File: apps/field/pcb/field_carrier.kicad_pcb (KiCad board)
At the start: 2 copper layers, 55 x 72 mm, 5 parts, among them J1 XIAO_ESP32C6, J3 E220_EV2, J4 ログ_UART0

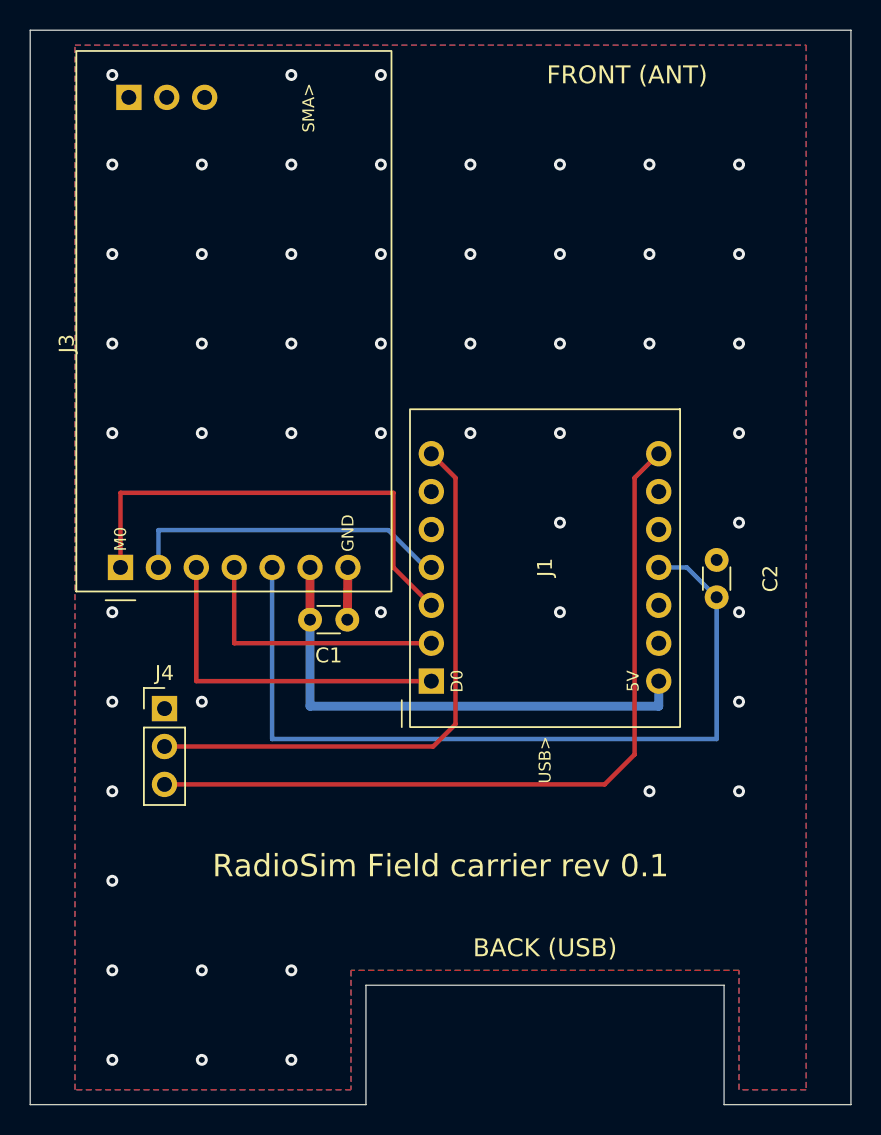
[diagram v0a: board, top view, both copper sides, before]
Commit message: feat(field): 台を EXPE7-4-6 に合わせて 55×45 で作り直し、表示の LED（D1〜D3・R1〜R6）を回路図と基板に足す
- 回路図: XIAO の D4・D5（920 の送信・受信）と D8・D9（2.4 の送信・受信）を 330 Ω 経由で
  D2・D3（OSRGHC3132A・赤＝送信・緑＝受信）へ。D1＝電源（5V から 1 kΩ×2・赤と黄緑で黄）。ERC 0 件
- 基板: 外形 55.0×45.0（切り欠きなし）。XIAO は基板の縁を y 45.5（受け口の面が背面パネルの外面と面一）。
  LED は背面の端（x 9.0・14.08・19.16・ランドの列 y 43.73）。抵抗は EV2 の下（EV2 は約 11 mm 浮く）に
  2.54 間隔＝LED の足から 7 ピンの隙間を真っすぐ通る。C1 は EV2 の 6・7 番の前、C2 は XIAO の右、J4 は右前
- 専用フットプリント: LED_D3.0mm-3_Horizontal_Staggered を足した（ランド 1.5＝背面端まで 0.5 を守る）。
  XIAO は受け口が縁から 2 mm 出る分を込み合いの枠に足し、シルクを台の上に収めた。EV2 の込み合いの枠は
  ソケットだけ（下に低い部品を置けるように）
- DRC（回路図との照合つき）＝違反 0・未配線 0・不一致 0

HARDWARE.md §3・§4 と wiring.svg はまだ直していない（次の作業）。

Co-Authored-By: Claude Opus 5.5 <noreply@anthropic.com>
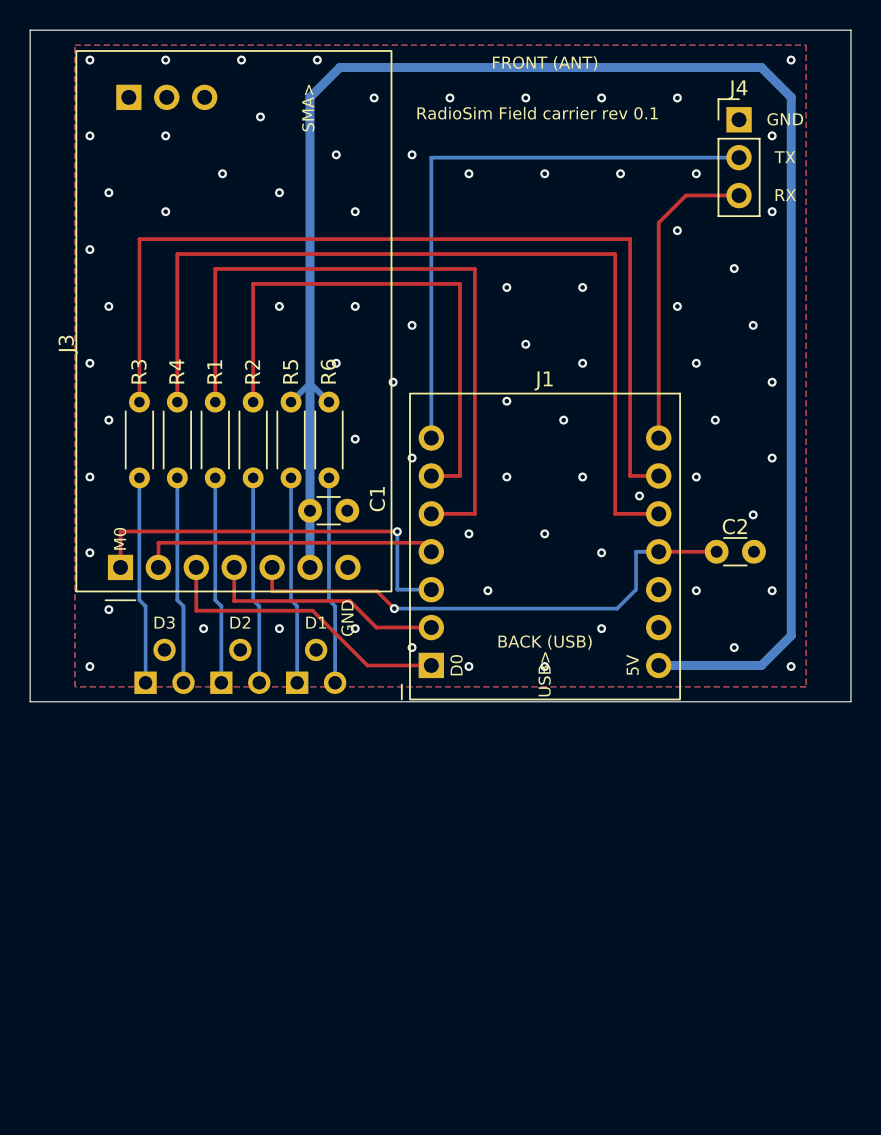
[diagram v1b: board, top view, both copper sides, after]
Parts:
- added D1: OSRGHC3132A, field_carrier:LED_D3.0mm-3_Horizontal_Staggered, F.Cu at (69.2, 73.7)
- added D2: OSRGHC3132A, field_carrier:LED_D3.0mm-3_Horizontal_Staggered, F.Cu at (64.1, 73.7)
- added D3: OSRGHC3132A, field_carrier:LED_D3.0mm-3_Horizontal_Staggered, F.Cu at (59.0, 73.7)
- added R1: 330, Resistor_THT:R_Axial_DIN0204_L3.6mm_D1.6mm_P5.08mm_Horizontal, F.Cu at (62.4, 54.9)
- added R2: 330, Resistor_THT:R_Axial_DIN0204_L3.6mm_D1.6mm_P5.08mm_Horizontal, F.Cu at (64.9, 54.9)
- added R3: 330, Resistor_THT:R_Axial_DIN0204_L3.6mm_D1.6mm_P5.08mm_Horizontal, F.Cu at (57.3, 54.9)
- added R4: 330, Resistor_THT:R_Axial_DIN0204_L3.6mm_D1.6mm_P5.08mm_Horizontal, F.Cu at (59.9, 54.9)
- added R5: 1k, Resistor_THT:R_Axial_DIN0204_L3.6mm_D1.6mm_P5.08mm_Horizontal, F.Cu at (67.5, 54.9)
- added R6: 1k, Resistor_THT:R_Axial_DIN0204_L3.6mm_D1.6mm_P5.08mm_Horizontal, F.Cu at (70.0, 54.9)
- moved J4 55.1 mm to (97.5, 36.0)
- moved C1 7.30 mm to (68.8, 62.2)
- moved C2 3.05 mm to (96.0, 65.0), turned to 0 degrees
- moved J1 1.05 mm to (84.5, 65.0)
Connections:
- J1 pad 10: unconnected-(J1B-D9-Pad10) -> /LED24_RX
- J1 pad 5: unconnected-(J1A-D4-Pad5) -> /LED920_TX
- J1 pad 6: unconnected-(J1A-D5-Pad6) -> /LED920_RX
- J1 pad 9: unconnected-(J1B-D8-Pad9) -> /LED24_TX
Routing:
- net +5V: track 34.3 -> 114.8 mm
- net /LED24_TX: track 0.00 -> 61.6 mm
- net /LED24_RX: track 0.00 -> 59.6 mm
- net /LED920_TX: track 0.00 -> 45.6 mm
- net /LED920_RX: track 0.00 -> 36.6 mm
- net /LOG_RX: track 53.2 -> 20.6 mm
- net /EV2_AUX: track 55.5 -> 34.9 mm, vias 0 -> 1
- net Net-(D1-A2): track 0.00 -> 13.9 mm
- net Net-(D3-A2): track 0.00 -> 13.9 mm
- net Net-(D2-A1): track 0.00 -> 13.9 mm
- net Net-(D3-A1): track 0.00 -> 13.9 mm
- net Net-(D1-A1): track 0.00 -> 13.9 mm
- net Net-(D2-A2): track 0.00 -> 13.9 mm
- net /EV2_M0: track 31.9 -> 27.1 mm, vias 0 -> 1
- net GND: track 3.50 -> 0.00 mm, vias 53 -> 75
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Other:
- board size 55 x 72 mm -> 55 x 45 mm
- board text added: "GND"
- board text added: "RX"
- board text added: "TX"

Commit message: feat(field): 表示の LED を 1 列のフットプリントへ置き換え、アノードと EV2_RXD を引き直す
- 専用フットプリントを LED_D3.0mm-3_Horizontal_Staggered（三角）から
  LED_D3.0mm-3_Horizontal_O2.54mm_Z2.0mm（足 3 本を 2.54 間隔の 1 列）へ。
  曲げる位置はつばから 2.54＝データシートの樹脂のはみ出し（1.5MAX）と外側の足の開き
  （つばの下 約 1.1 で 2.54 に開き終わる）の両方から外れる。軸の高さ Z 2.0 とつばを
  背面パネルの内面に当てる位置は前のまま
- 配置: D3・D2・D1＝中心 x 8.45・15.25・22.05、ランドの列 y 42.46（6.8 間隔・ランド 1.5）。
  D3 の穴の縁 6.85 は穴あけ範囲（有効寸法 41.5）の左端 6.75 まで 0.1。外側のフレームの
  窓の縁（図面 p002 の正面図を画素で測った・LED の軸の高さで x 5.59）までは 約 1.26
- 裏: アノード 6 本は y 41.4 から 45° でそろえて寄せ、EV2 の 7 ピンの隙間を抜けて抵抗へ
  （抵抗の並びは前のまま）。表: EV2_RXD は XIAO の 1 番から斜めに下げ、LED のランドの前
  （y 40.93）を通って TXD の外を回る
- 新しい線に乗った GND の縫いビア 3 つを除いた（75 → 72）。XIAO の込み合いの枠は
  EV2 と同じくソケットの 2 列だけにした（モジュールは約 11 mm 浮く・LED は高さ 約 3.9）
- DRC（回路図との照合つき）＝違反 0・未配線 0・不一致 0。ERC 0

Co-Authored-By: Claude Opus 5.5 <noreply@anthropic.com>
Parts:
- D1, D2, D3: footprint field_carrier:LED_D3.0mm-3_Horizontal_Staggered -> field_carrier:LED_D3.0mm-3_Horizontal_O2.54mm_Z2.0mm
- moved D1 3.16 mm to (72.0, 72.5)
- moved D2 1.73 mm to (65.2, 72.5)
- moved D3 1.38 mm to (58.5, 72.5)
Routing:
- net Net-(D2-A1): track 13.9 -> 12.6 mm
- net Net-(D3-A2): track 13.9 -> 12.9 mm
- net Net-(D3-A1): track 13.9 -> 13.0 mm
- net Net-(D1-A1): track 13.9 -> 13.3 mm
- net GND: vias 75 -> 72

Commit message: feat(field): 台を背面パネルまで伸ばし（55.0×46.0）、溝に入る両端の帯を GND として露出してケースを接地する
- 台の後端 45.0 → 46.0（前後のパネルの内面どうし）＝ケーブルを挿す力を XIAO でなくパネルで受ける
- 溝に入る帯（両端から 0.5〜2.5 mm）を表裏とも GND のベタにしてレジストを抜き、縫いビアを片側 9 個足した
- J3 の番号を EV2 の外形の内側へ移した（溝の帯に掛かっていた）
- HARDWARE.md の §4 に台とケースの行と「台とケース」の小節、wiring.svg に「台とケース」の節を足した

Co-Authored-By: Claude Opus 5.5 <noreply@anthropic.com>
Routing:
- net GND: vias 72 -> 90
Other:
- board size 55 x 45 mm -> 55 x 46 mm
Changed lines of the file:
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@@
 		(descr "CLEALINK E220-900T22S(JP)-EV2 (board 10060-V1.1), 36.00x20.90 mm. Pins 1-7 = M0 M1 RXD TXD AUX VCC GND; pins 8-10 = GND through-holes, 31.50 mm from the pin row. No mounting holes. Courtyard covers the sockets only: the module sits about 11 mm above the carrier, so low parts (resistors, C1) may go under it.")
 		(property "Reference" "J3"
-			(at 15 -3.6 90)
+			(at 26 -1.75 90)
 			(layer "F.SilkS")
 			(effects
@@
 		)
 	)
+	(gr_rect
+		(start 50.5 30.5)
+		(end 52.5 75.5)
+		(stroke
+			(width 0)
+			(type solid)
+		)
+		(fill yes)
+		(layer "F.Mask")
+	)
+	(gr_rect
+		(start 102.5 30.5)
+		(end 104.5 75.5)
+		(stroke
+			(width 0)
+			(type solid)
+		)
+		(fill yes)
+		(layer "F.Mask")
+	)
+	(gr_rect
+		(start 50.5 30.5)
+		(end 52.5 75.5)
+		(stroke
+			(width 0)
+			(type solid)
+		)
+		(fill yes)
+		(layer "B.Mask")
+	)
+	(gr_rect
+		(start 102.5 30.5)
+		(end 104.5 75.5)
+		(stroke
+			(width 0)
+			(type solid)
+		)
+		(fill yes)
+		(layer "B.Mask")
+	)
 	(gr_line
 		(start 50 30)
@@
 	)
 	(gr_line
-		(start 50 75)
+		(start 50 76)
 		(end 50 30)
 		(stroke
@@
 	(gr_line
 		(start 105 30)
-		(end 105 75)
+		(end 105 76)
 		(stroke
 			(width 0.05)
@@
 	)
 	(gr_line
-		(start 105 75)
-		(end 50 75)
+		(start 105 76)
+		(end 50 76)
 		(stroke
 			(width 0.05)
@@
 	)
 	(via
+		(at 103.5 38)
+		(size 0.6)
+		(drill 0.3)
+		(layers "F.Cu" "B.Cu")
+		(net "GND")
+	)
+	(via
 		(at 65.43 35.81)
 		(size 0.6)
@@
 	)
 	(via
+		(at 103.5 63)
+		(size 0.6)
+		(drill 0.3)
+		(layers "F.Cu" "B.Cu")
+		(net "GND")
+	)
+	(via
+		(at 51.5 33)
+		(size 0.6)
+		(drill 0.3)
+		(layers "F.Cu" "B.Cu")
+		(net "GND")
+	)
+	(via
+		(at 51.5 68)
+		(size 0.6)
+		(drill 0.3)
+		(layers "F.Cu" "B.Cu")
+		(net "GND")
+	)
+	(via
 		(at 94.64 59.94)
 		(size 0.6)
@@
 	)
 	(via
+		(at 103.5 73)
+		(size 0.6)
+		(drill 0.3)
+		(layers "F.Cu" "B.Cu")
+		(net "GND")
+	)
+	(via
 		(at 75.59 38.35)
 		(size 0.6)
@@
 	)
 	(via
+		(at 103.5 33)
+		(size 0.6)
+		(drill 0.3)
+		(layers "F.Cu" "B.Cu")
+		(net "GND")
+	)
+	(via
 		(at 99.72 37.08)
 		(size 0.6)
@@
 	)
 	(via
+		(at 51.5 53)
+		(size 0.6)
+		(drill 0.3)
+		(layers "F.Cu" "B.Cu")
+		(net "GND")
+	)
+	(via
 		(at 87.02 47.24)
 		(size 0.6)
@@
 	)
 	(via
+		(at 51.5 43)
+		(size 0.6)
+		(drill 0.3)
+		(layers "F.Cu" "B.Cu")
+		(net "GND")
+	)
+	(via
+		(at 103.5 43)
+		(size 0.6)
+		(drill 0.3)
+		(layers "F.Cu" "B.Cu")
+		(net "GND")
+	)
+	(via
+		(at 103.5 58)
+		(size 0.6)
+		(drill 0.3)
+		(layers "F.Cu" "B.Cu")
+		(net "GND")
+	)
+	(via
+		(at 51.5 58)
+		(size 0.6)
+		(drill 0.3)
+		(layers "F.Cu" "B.Cu")
+		(net "GND")
+	)
+	(via
 		(at 79.4 72.64)
 		(size 0.6)
@@
 	)
 	(via
+		(at 51.5 73)
+		(size 0.6)
+		(drill 0.3)
+		(layers "F.Cu" "B.Cu")
+		(net "GND")
+	)
+	(via
 		(at 75.59 49.78)
 		(size 0.6)
@@
 	)
 	(via
+		(at 51.5 38)
+		(size 0.6)
+		(drill 0.3)
+		(layers "F.Cu" "B.Cu")
+		(net "GND")
+	)
+	(via
 		(at 54 32)
 		(size 0.6)
@@
 	)
 	(via
+		(at 103.5 53)
+		(size 0.6)
+		(drill 0.3)
+		(layers "F.Cu" "B.Cu")
+		(net "GND")
+	)
+	(via
 		(at 61.62 70.1)
 		(size 0.6)
@@
 	)
 	(via
+		(at 51.5 48)
+		(size 0.6)
+		(drill 0.3)
+		(layers "F.Cu" "B.Cu")
+		(net "GND")
+	)
+	(via
 		(at 94.64 67.56)
 		(size 0.6)
@@
 	)
 	(via
+		(at 51.5 63)
+		(size 0.6)
+		(drill 0.3)
+		(layers "F.Cu" "B.Cu")
+		(net "GND")
+	)
+	(via
+		(at 103.5 68)
+		(size 0.6)
+		(drill 0.3)
+		(layers "F.Cu" "B.Cu")
+		(net "GND")
+	)
+	(via
 		(at 83.21 51.05)
 		(size 0.6)
@@
 	(via
 		(at 71.78 48.51)
+		(size 0.6)
+		(drill 0.3)
+		(layers "F.Cu" "B.Cu")
+		(net "GND")
+	)
+	(via
+		(at 103.5 48)
 		(size 0.6)
 		(drill 0.3)
@@
 		(polygon
 			(pts
-				(xy 53 31) (xy 102 31) (xy 102 74) (xy 53 74)
+				(xy 50.5 31) (xy 104.5 31) (xy 104.5 75) (xy 50.5 75)
 			)
 		)
@@
 		(polygon
 			(pts
-				(xy 53 31) (xy 102 31) (xy 102 74) (xy 53 74)
-			)
-		)
+				(xy 50.5 31) (xy 104.5 31) (xy 104.5 75) (xy 50.5 75)
+			)
+		)
